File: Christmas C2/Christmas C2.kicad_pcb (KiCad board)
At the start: 2 copper layers, 94.2 x 94.2 mm, 11 parts, among them J1 A_LEFT, J2 A_RIGHT, J3 B_LEFT, J4 B_RIGHT, J5 PWR_EXT, M1 Mounting, M2 Mounting, M3 Mounting, M4 Mounting

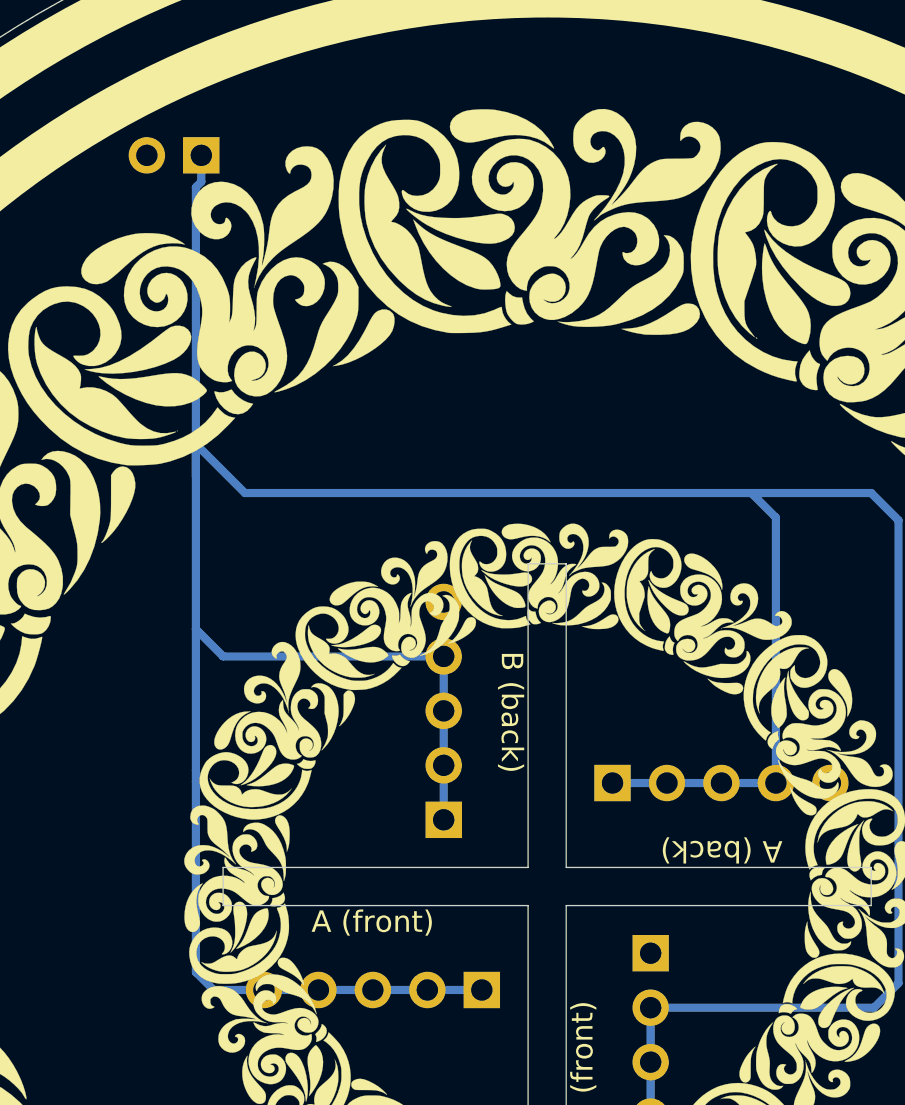
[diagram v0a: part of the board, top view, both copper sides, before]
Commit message: Added MicroUSB breakout adapter and battery option to static board
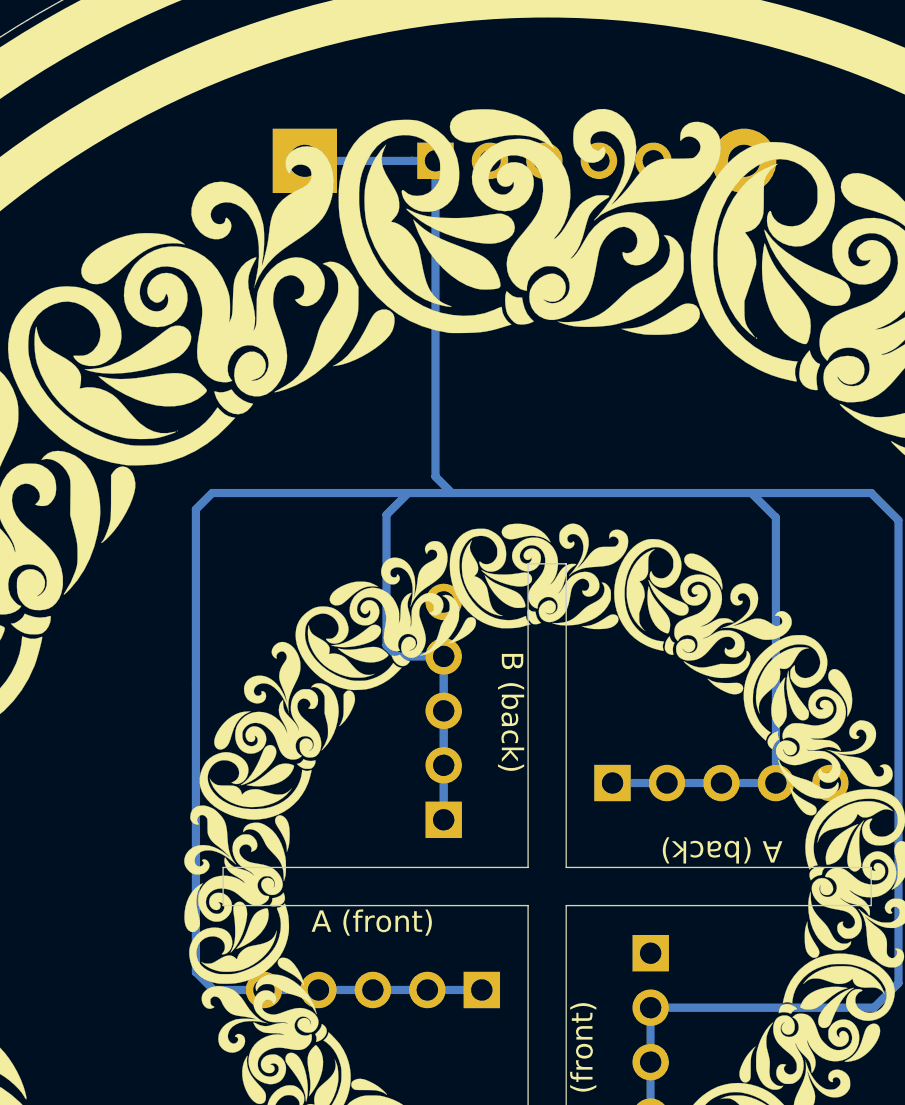
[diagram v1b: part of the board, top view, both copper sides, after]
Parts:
- removed J5: PWR_EXT, Pin_Headers:Pin_Header_Straight_1x02_Pitch2.54mm
- added A1: MicroUSB, christmas:microusb_breakout, B.Cu at (104.6, 116.8)
- added BT1: CR2032, Battery_Holders:Keystone_103_1x20mm-CoinCell, B.Cu at (93.5, 116.8)
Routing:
- net VCC: track 170.0 -> 171.7 mm
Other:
- board text removed: "GND"
- board text removed: "VCC"
